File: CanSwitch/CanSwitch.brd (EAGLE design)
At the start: 61.5 x 72 mm, 17 parts

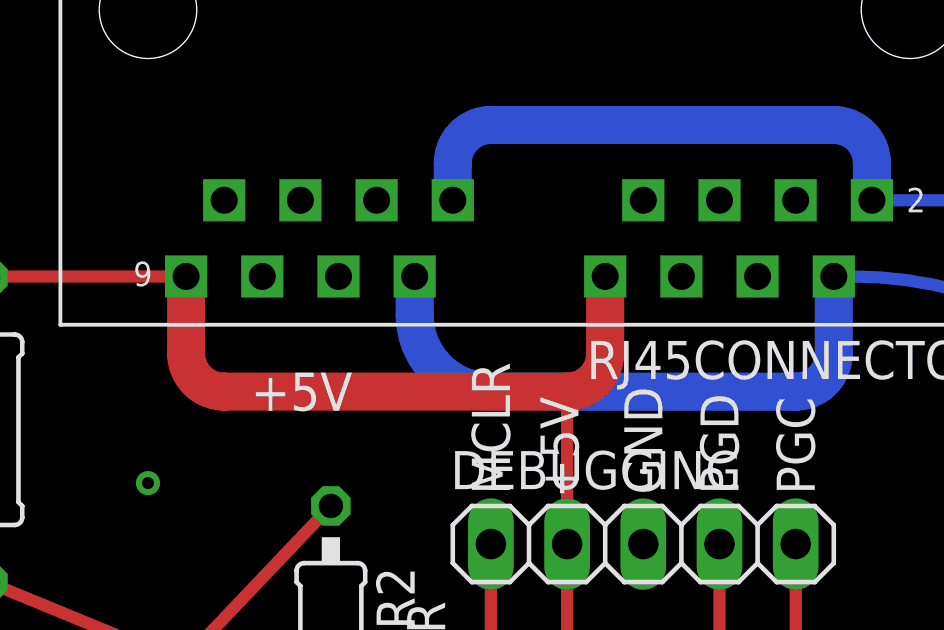
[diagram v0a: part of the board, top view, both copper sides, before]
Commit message: #11 fixing RJ45 connector - connecting unused pins to +5V and GND
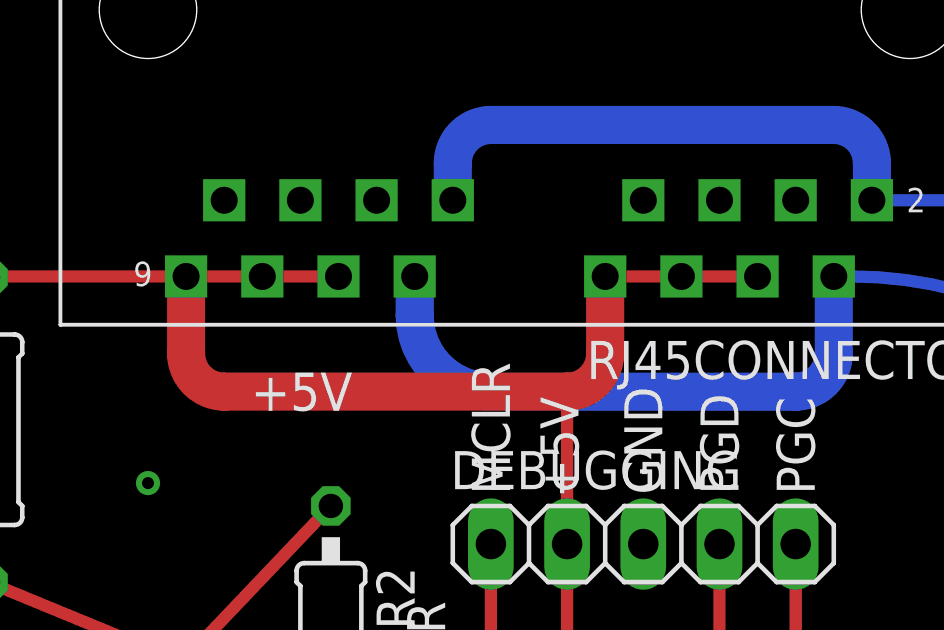
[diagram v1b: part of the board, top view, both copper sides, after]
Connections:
- net +5V: now also RJ45CONNECTOR.RJ4515, RJ45CONNECTOR.RJ4517, RJ45CONNECTOR.RJ4525, RJ45CONNECTOR.RJ4527
- net GND: now also RJ45CONNECTOR.RJ4516, RJ45CONNECTOR.RJ4526
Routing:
- net +5V: track 83.5 -> 93.7 mm
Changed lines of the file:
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@@
 <?xml version="1.0" encoding="utf-8"?>
 <!DOCTYPE eagle SYSTEM "eagle.dtd">
-<eagle version="7.6.0">
+<eagle version="7.7.0">
 <drawing>
 <settings>
@@
 <contactref element="C2" pad="1"/>
 <contactref element="MCP2561" pad="VDD"/>
-<contactref element="RJ45CONNECTOR" pad="RJ4519"/>
 <contactref element="RJ45CONNECTOR" pad="RJ4529"/>
 <contactref element="DEBUGGING" pad="2"/>
@@
 <wire x1="14.097" y1="50.546" x2="15.367" y2="49.276" width="1.27" layer="1" curve="90"/>
 <wire x1="15.367" y1="49.276" x2="26.797" y2="49.276" width="1.27" layer="1"/>
-<wire x1="28.067" y1="53.116" x2="28.067" y2="50.546" width="1.27" layer="1"/>
 <wire x1="28.067" y1="50.546" x2="26.797" y2="49.276" width="1.27" layer="1" curve="-90"/>
 <wire x1="26.797" y1="49.276" x2="26.797" y2="44.196" width="0.4064" layer="1"/>
@@
 <wire x1="37.338" y1="17.526" x2="40.513" y2="20.701" width="0.4064" layer="1" curve="90"/>
 <wire x1="40.513" y1="20.701" x2="40.513" y2="32.766" width="0.4064" layer="1"/>
+<contactref element="RJ45CONNECTOR" pad="RJ4515"/>
+<contactref element="RJ45CONNECTOR" pad="RJ4527"/>
+<contactref element="RJ45CONNECTOR" pad="RJ4517"/>
+<wire x1="16.637" y1="53.116" x2="14.097" y2="53.116" width="0.4064" layer="1"/>
+<wire x1="30.607" y1="53.116" x2="33.147" y2="53.116" width="0.4064" layer="1"/>
+<contactref element="RJ45CONNECTOR" pad="RJ4519"/>
+<contactref element="RJ45CONNECTOR" pad="RJ4525"/>
+<wire x1="16.637" y1="53.116" x2="19.177" y2="53.116" width="0.4064" layer="1"/>
+<wire x1="28.067" y1="53.116" x2="30.607" y2="53.116" width="0.4064" layer="1"/>
+<wire x1="28.067" y1="50.546" x2="28.067" y2="53.116" width="1.27" layer="1"/>
 </signal>
 <signal name="GND">
@@
 <contactref element="RJ45CONNECTOR" pad="RJ4514"/>
 <contactref element="RJ45CONNECTOR" pad="RJ4528"/>
-<contactref element="RJ45CONNECTOR" pad="RJ4518"/>
-<contactref element="RJ45CONNECTOR" pad="RJ4524"/>
 <contactref element="DEBUGGING" pad="3"/>
 <contactref element="C3" pad="1"/>
@@
 <via x="20.193" y="10.033" extent="1-16" drill="0.4" shape="square"/>
 <via x="3.683" y="49.022" extent="1-16" drill="0.4" shape="square"/>
+<contactref element="RJ45CONNECTOR" pad="RJ4518"/>
+<contactref element="RJ45CONNECTOR" pad="RJ4524"/>
+<contactref element="RJ45CONNECTOR" pad="RJ4526"/>
+<contactref element="RJ45CONNECTOR" pad="RJ4516"/>
 </signal>
 <signal name="N$2">

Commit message: #13 connect RC3 of chip and STBY of transceiver, no route yet in board until the new inputs are added
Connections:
- new net STBY: CHIP.14, MCP2561.STBY
- net GND: no longer MCP2561.STBY
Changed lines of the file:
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@@
 <contactref element="STATUSLED" pad="A"/>
 <contactref element="MCP2561" pad="VSS"/>
-<contactref element="MCP2561" pad="STBY"/>
 <contactref element="SWITCHINPUT" pad="GND"/>
 <contactref element="CHIP" pad="8"/>
@@
 <wire x1="19.177" y1="14.986" x2="24.257" y2="14.986" width="0.4064" layer="1"/>
 </signal>
+<signal name="STBY">
+<contactref element="MCP2561" pad="STBY"/>
+<contactref element="CHIP" pad="14"/>
+<wire x1="24.257" y1="4.826" x2="53.911" y2="37.846" width="0" layer="19" extent="1-1"/>
+</signal>
 </signals>

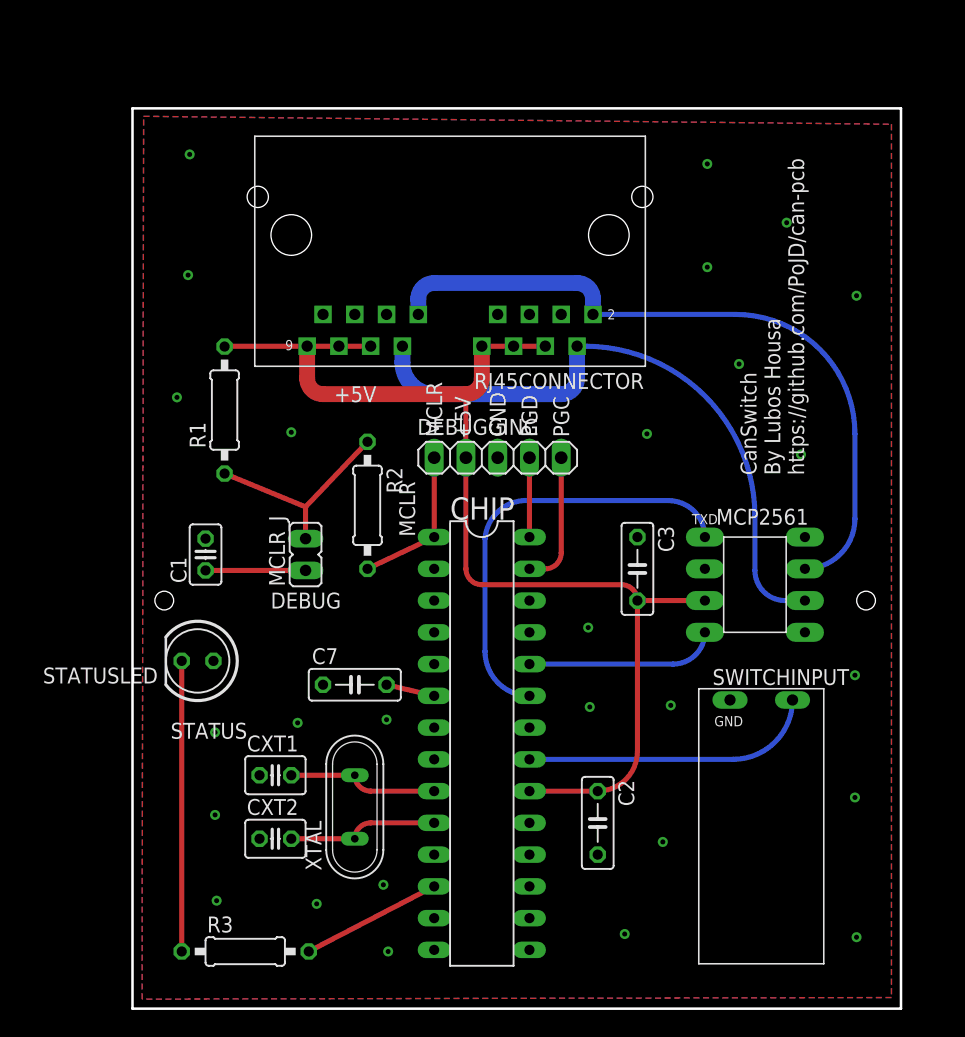
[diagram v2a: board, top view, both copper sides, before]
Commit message: #8 support for 8 independent inputs  - dropped old switch input and replaced with RJ45 connector  - moved components around, moved transceiver down to the bottom and the  new RJ45 in the middle close to the chip  - re-routed related signals, made +5V thicker  - RX and TX routed to RC pins afterall, added labels too  - Eagle now reports clearance on the RJ45 socket, need to check allpcb  whether that is not too close for them to manufacter. probably is too  close, need to fix that next time
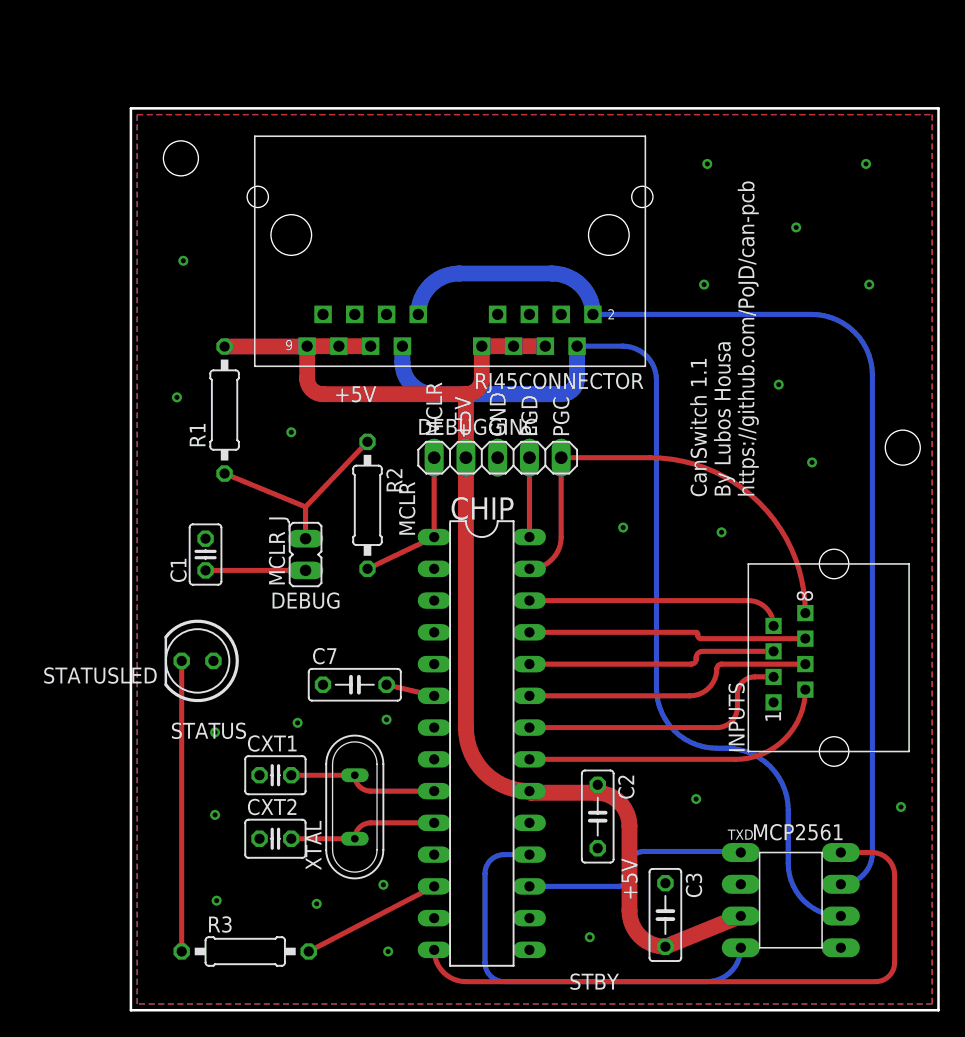
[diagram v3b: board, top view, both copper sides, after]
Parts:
- removed SWITCHINPUT: PTRAK700250GME, PoJD:PTR_AK700_2_5.0
- added INPUTS: WEBP88_SSINGLE, PoJD:WEBP88_RJ45_SINGLE
- moved C3 27.8 mm to (42.8, 7.62)
- moved MCP2561 25.4 mm to (52.8, 8.80)
- moved C2 0.51 mm to (37.3, 15.5)
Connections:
- net PGD renamed PGD/INPUT8
- removed net INPUT: CHIP.21, SWITCHINPUT.INPUT
- removed net PGC: CHIP.27, DEBUGGING.5
- new net INPUT1: CHIP.21, INPUTS.RJ45_2
- new net INPUT2: CHIP.22, INPUTS.RJ45_3
- new net INPUT3: CHIP.23, INPUTS.RJ45_4
- new net INPUT4: CHIP.24, INPUTS.RJ45_5
- new net INPUT5: CHIP.25, INPUTS.RJ45_6
- new net INPUT6: CHIP.26, INPUTS.RJ45_7
- new net PGC/INPUT7: CHIP.27, DEBUGGING.5, INPUTS.RJ45_8
- net GND: now also INPUTS.RJ45_1; no longer SWITCHINPUT.GND
- net RXD: now also CHIP.18; no longer CHIP.24
- net TXD: now also CHIP.17; no longer CHIP.23
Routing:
- net STBY: track 0.00 -> 50.6 mm
- net PGC/INPUT7: track 0.00 -> 34.6 mm
- net CANH: track 54.9 -> 82.8 mm
- net CANL: track 48.6 -> 76.3 mm
- net INPUT1: track 0.00 -> 24.4 mm
- net INPUT3: track 0.00 -> 23.1 mm
- net INPUT: track 23.0 -> 0.00 mm
- net INPUT5: track 0.00 -> 22.4 mm
- net INPUT2: track 0.00 -> 21.8 mm
- net INPUT6: track 0.00 -> 20.4 mm
- net INPUT4: track 0.00 -> 20.0 mm
- net RXD: track 15.1 -> 33.5 mm
- net TXD: track 34.0 -> 18.5 mm
- net PGC: track 10.7 -> 0.00 mm
- net +5V: track 93.7 -> 98.6 mm
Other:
- board size 61.5 x 72 mm -> 64.6 x 72.1 mm
- board text added: "CANRX"
- board text added: "CANTX"
- board text added: "CanSwitch 1.1 By Lubos Housa https://github.com/PoJD/can-pcb"
- board text added: "STBY"
- board text removed: "CanSwitch By Lubos Housa https://github.com/PoJD/can-pcb"

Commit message: #8 fine tuning RJ45 connections on the board  - clearance errors fixed, moved components a tiny bit more, transceiver  so that both CAN lines can be routed on the rights from the inputs and  bottom layer  - 2 rear inputs routed on bottom layer to avoid clearance errors  - little edits elsewhere too, e.g. using RXD and TXD lines instead of  CANRX and CANTX
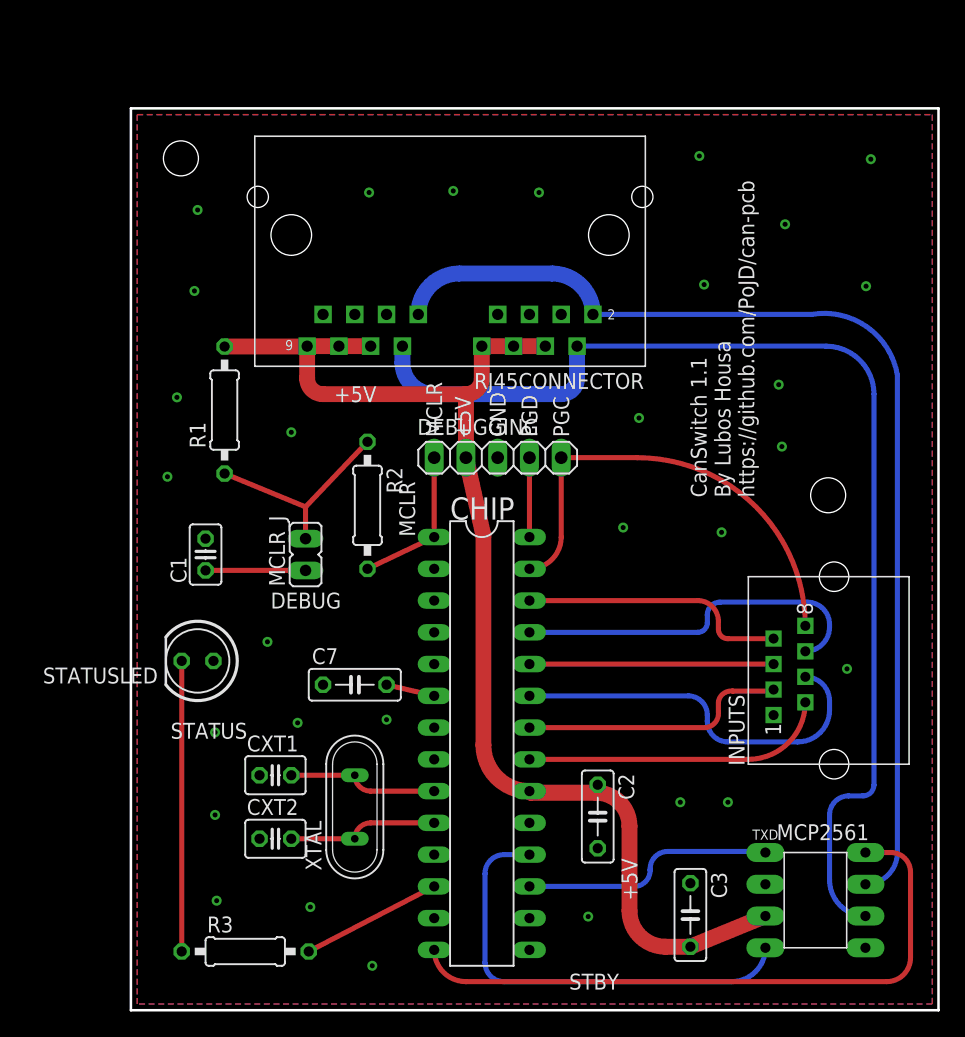
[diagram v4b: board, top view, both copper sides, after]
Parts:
- moved C3 2.00 mm to (44.8, 7.62)
- moved MCP2561 1.97 mm to (54.8, 8.80)
- moved INPUTS 1.02 mm to (55.8, 27.2)
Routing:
- net CANL: track 76.3 -> 89.8 mm
- net INPUT3: track 23.1 -> 30.3 mm
- net INPUT5: track 22.4 -> 29.1 mm
- net RXD: track 33.5 -> 35.5 mm
- net TXD: track 18.5 -> 20.1 mm
- net CANH: track 82.8 -> 84.4 mm
- net +5V: track 98.6 -> 100.2 mm
- net INPUT6: track 20.4 -> 21.2 mm
- net INPUT2: track 21.8 -> 21.3 mm
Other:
- board text added: "RXD"
- board text added: "TXD"
- board text removed: "CANRX"
- board text removed: "CANTX"
